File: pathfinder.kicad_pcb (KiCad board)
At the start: 2 copper layers, 67.5 x 69.1 mm, 20 parts, among them SW1 SW_Push, SW2 SW_Push, SW3 SW_Push, SW4 SW_Push, SW5 SW_Push, SW6 SW_Push, U1 XIAO-RP2040-DIP, U2 OLED_0.91_128x32

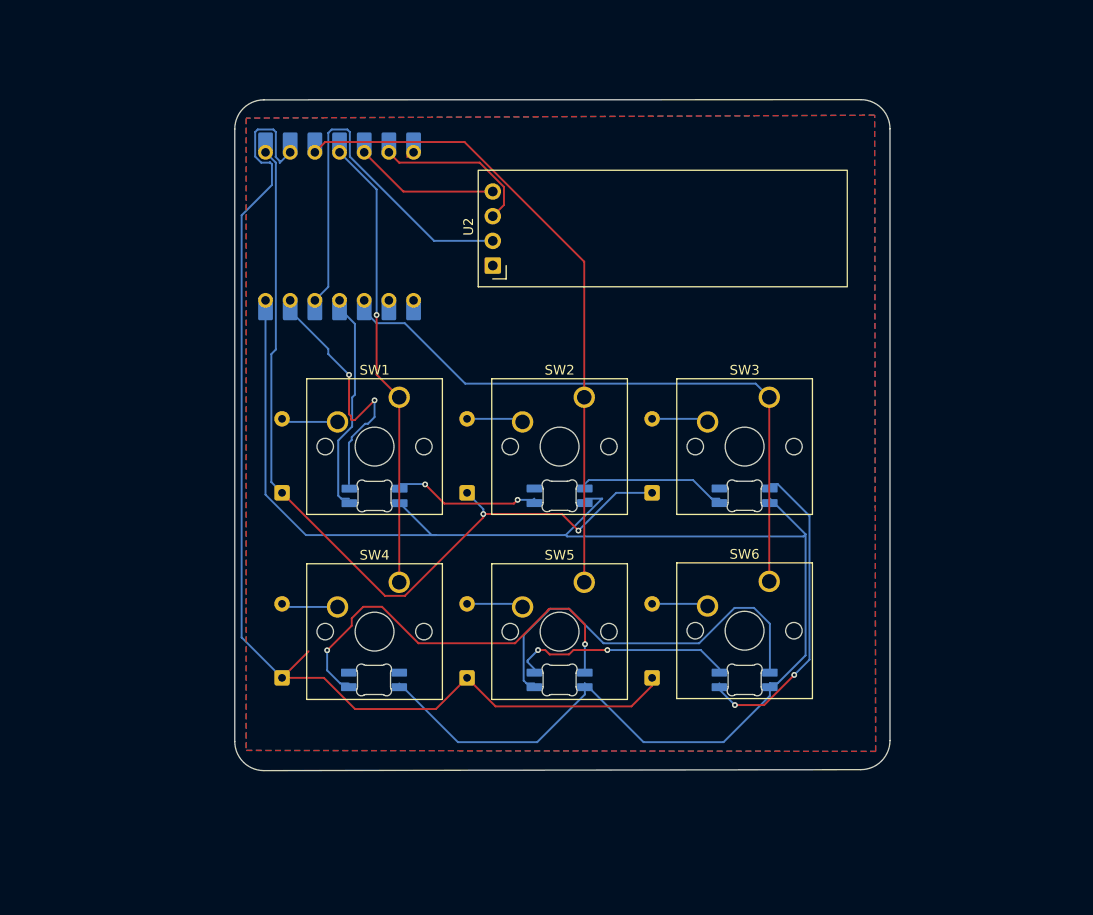
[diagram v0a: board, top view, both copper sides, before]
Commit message: fix
deleted my whole folder mb
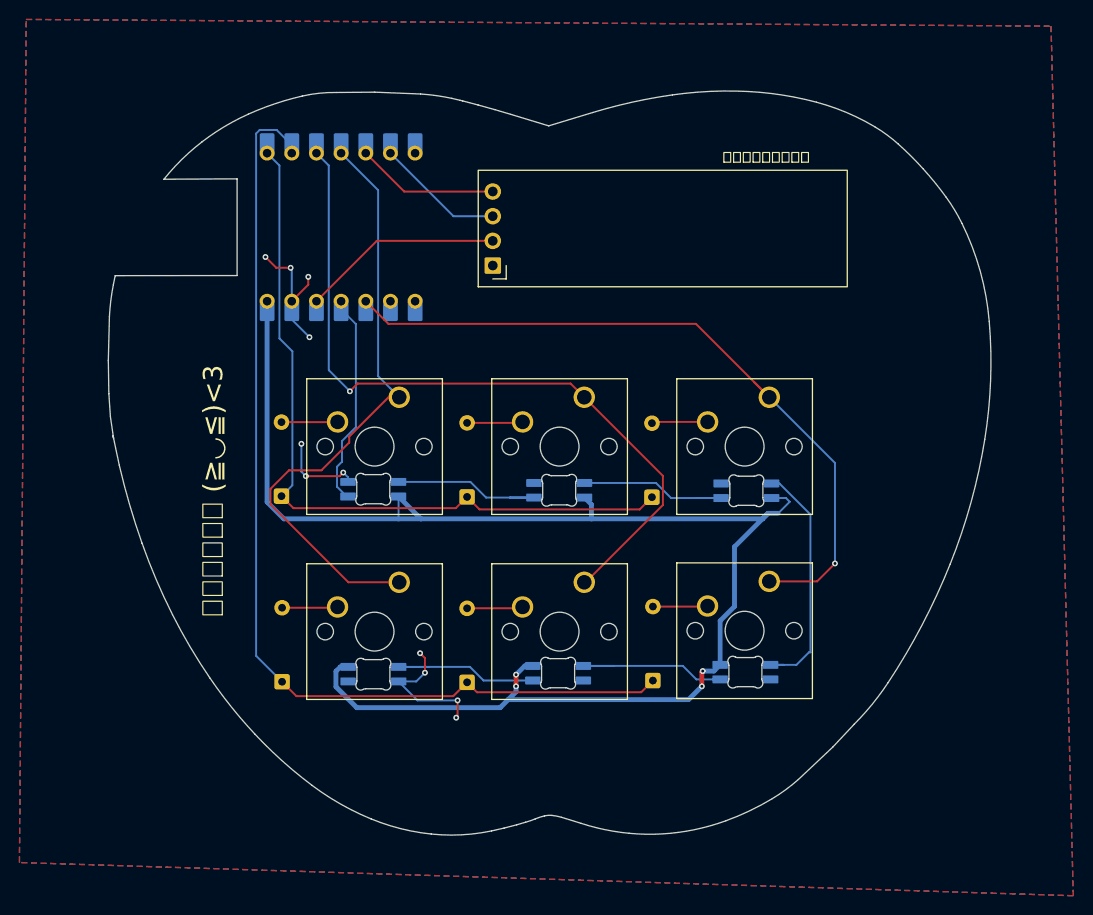
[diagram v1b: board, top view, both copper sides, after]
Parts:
- D10, D11, D12, D7, D8, D9: footprint Hackclub Footprints:MX_SK6812MINI-E_REV -> SK6812 Mini-E:SK6812MINI-E_fixed
- U1: footprint XIAO_Series_Footprints:XIAO-RP2040-DIP -> XIAO RP SERIES:XIAO-RP2040-DIP
- moved D12 4.59 mm to (137.6, 105.9)
- moved D11 4.49 mm to (156.6, 105.8)
- moved D9 4.46 mm to (176.0, 86.8), turned to 180 degrees
- moved D8 4.41 mm to (156.7, 86.8), turned to 180 degrees
- moved D10 4.38 mm to (175.9, 105.7)
- moved D7 4.29 mm to (137.6, 86.7), turned to 180 degrees
- moved D5 0.46 mm to (147.2, 106.7)
- moved D3 0.45 mm to (166.3, 87.6)
- moved D2 0.42 mm to (147.2, 87.6)
- moved D4 0.40 mm to (128.2, 106.6)
- moved D1 0.34 mm to (128.1, 87.5)
- moved D6 0.29 mm to (166.4, 106.5)
- moved U1 0.18 mm to (134.3, 59.8), turned to -90 degrees
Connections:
- U1 pad 7: ENC_A -> unconnected-(U1-GPIO0/TX-Pad7)
- U1 pad 8: ENC_B -> unconnected-(U1-GPIO1/RX-Pad8)_1
- U1 pad 9: ENC_SW -> unconnected-(U1-GPIO2/SCK-Pad9)_1
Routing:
- net Net-(D11-DOUT): track 42.0 -> 18.1 mm, vias 2 -> 0
- net Net-(D10-DOUT): track 40.6 -> 18.5 mm
- net VCC: track 41.1 -> 21.6 mm
- net COL1: track 46.8 -> 65.4 mm, vias 1 -> 0
- net GND: track 50.5 -> 36.9 mm, vias 4 -> 11
- net COL2: track 66.3 -> 77.7 mm, vias 0 -> 1
- net ROW2: track 115.3 -> 104.0 mm
- net COL3: track 65.4 -> 76.1 mm, vias 0 -> 1
- net ROW1: track 87.5 -> 77.9 mm, vias 2 -> 0
- net 5V: track 161.8 -> 154.9 mm, vias 0 -> 4
- net Net-(D10-DIN): track 32.8 -> 25.9 mm, vias 2 -> 0
- net SCL: track 16.8 -> 14.1 mm
- net Net-(D8-DOUT): track 14.8 -> 17.3 mm
- net Net-(D7-DOUT): track 14.9 -> 17.1 mm, vias 2 -> 0
- net ENC_SW: track 1.08 -> 0.00 mm
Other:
- board size 67.5 x 69.1 mm -> 90.9 x 76.6 mm
- board text added: "好好学习，天天向上"
- board text added: "电路也有心跳 (≧◡≦)<3"
